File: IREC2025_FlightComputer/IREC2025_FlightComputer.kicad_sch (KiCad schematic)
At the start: 69 parts, among them J1 Molex Microfit, J2 BOOT0, J3 Companion, J5 SWD, Q1 SI7232DN-T1-GE3, U1 STM32U575VGTx, U2 NRVB120VLSFT1G, U4 NRVB120VLSFT1G, U5 LP5912Q3.3DRVRQ1, U8 TPS62153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

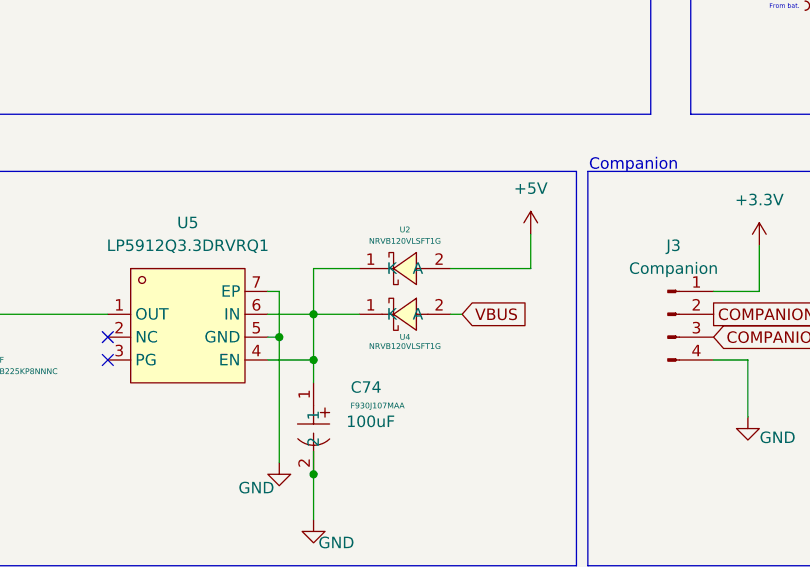
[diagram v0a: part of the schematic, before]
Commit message: Added silkscreen + Layout Minorchange
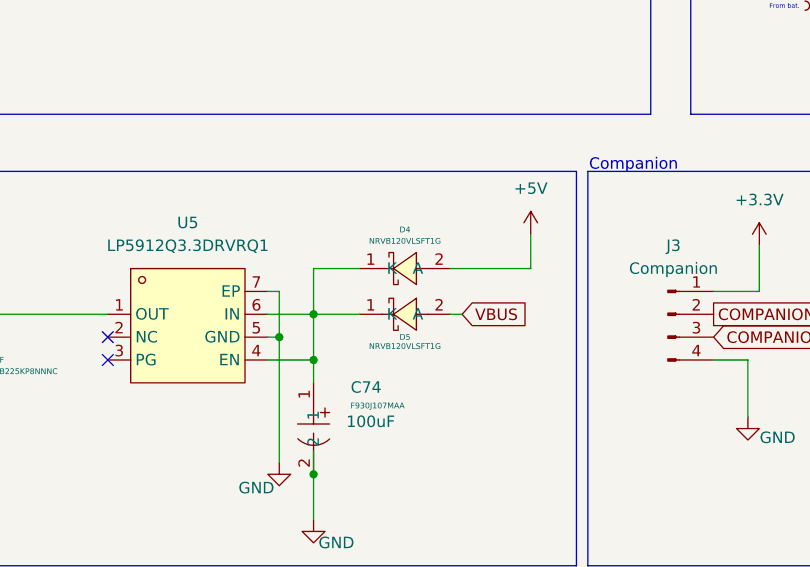
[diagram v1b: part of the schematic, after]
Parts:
- renumbered U2 to D4, U4 to D5
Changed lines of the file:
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@@
 		(on_board yes)
 		(dnp no)
-		(property "Reference" "U4"
+		(property "Reference" "D5"
 			(at 238.76 138.43 0)
 			(effects
@@
 			(project "IREC2025_FlightComputer"
 				(path "/d402aac1-6798-4745-a2ce-fc3f8e4c9afb"
-					(reference "U4")
+					(reference "D5")
 					(unit 1)
 				)
@@
 		(on_board yes)
 		(dnp no)
-		(property "Reference" "U2"
+		(property "Reference" "D4"
 			(at 238.76 126.492 0)
 			(effects
@@
 			(project ""
 				(path "/d402aac1-6798-4745-a2ce-fc3f8e4c9afb"
-					(reference "U2")
+					(reference "D4")
 					(unit 1)
 				)

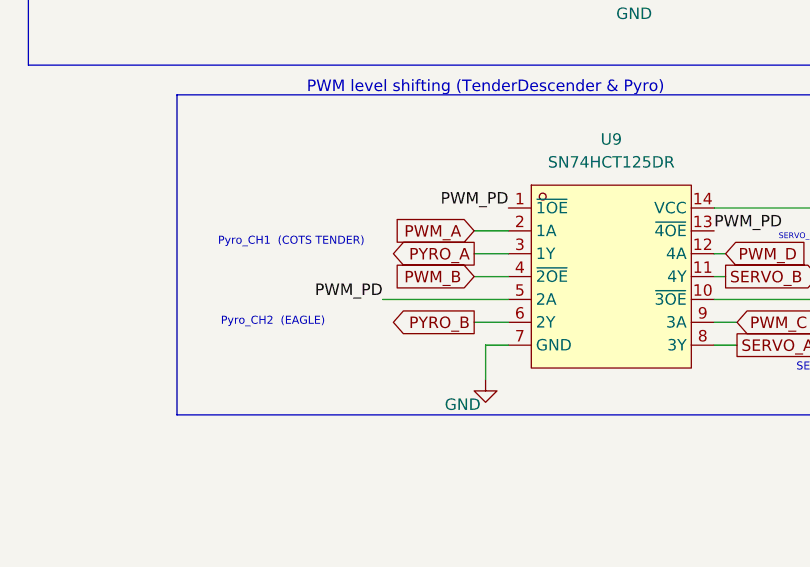
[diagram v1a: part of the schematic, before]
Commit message: Schematics minor fixes
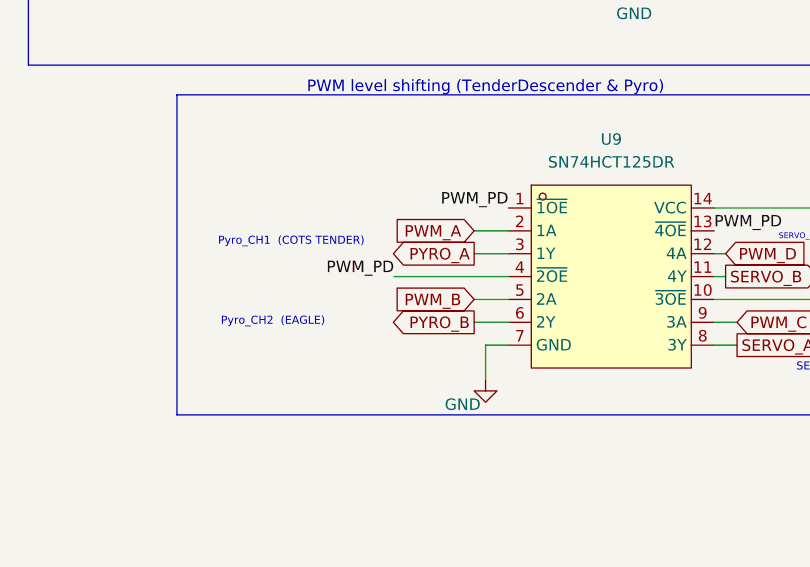
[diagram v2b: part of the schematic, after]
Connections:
- net PWM_B: now also U9.5 (2A); no longer U9.4 (~{2OE})
- net PWM_PD: now also U9.4 (~{2OE}); no longer U9.5 (2A)
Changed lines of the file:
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@@
 	(wire
 		(pts
-			(xy 52.07 212.09) (xy 66.04 212.09)
-		)
-		(stroke
-			(width 0)
-			(type default)
-		)
-	)
-	(wire
-		(pts
 			(xy 322.58 27.94) (xy 322.58 30.48)
 		)
@@
 	(wire
 		(pts
+			(xy 53.34 209.55) (xy 66.04 209.55)
+		)
+		(stroke
+			(width 0)
+			(type default)
+		)
+	)
+	(wire
+		(pts
 			(xy 182.88 104.14) (xy 182.88 106.68)
 		)
@@
 	(wire
 		(pts
-			(xy 62.23 209.55) (xy 66.04 209.55)
-		)
-		(stroke
-			(width 0)
-			(type default)
-		)
-	)
-	(wire
-		(pts
 			(xy 189.23 144.78) (xy 189.23 152.4)
 		)
@@
 	(wire
 		(pts
+			(xy 62.23 212.09) (xy 66.04 212.09)
+		)
+		(stroke
+			(width 0)
+			(type default)
+		)
+	)
+	(wire
+		(pts
 			(xy 121.92 213.36) (xy 121.92 215.9)
 		)
@@
 	)
 	(label "PWM_PD"
-		(at 52.07 212.09 180)
+		(at 53.34 209.55 180)
 		(effects
 			(font
@@
 	(global_label "PWM_B"
 		(shape input)
-		(at 62.23 209.55 180)
+		(at 62.23 212.09 180)
 		(fields_autoplaced yes)
 		(effects
@@
 		)
 		(property "Intersheetrefs" "${INTERSHEET_REFS}"
-			(at 52.8344 209.55 0)
+			(at 52.8344 212.09 0)
 			(effects
 				(font

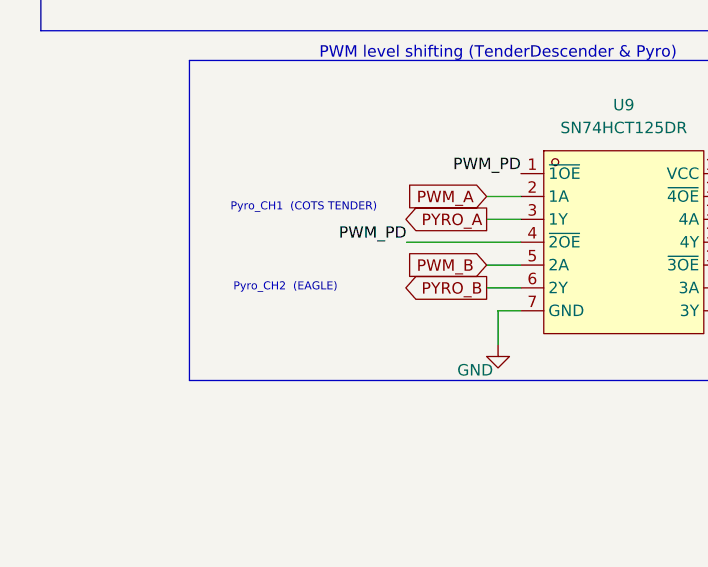
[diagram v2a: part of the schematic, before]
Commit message: USB Differentials matched to 90R
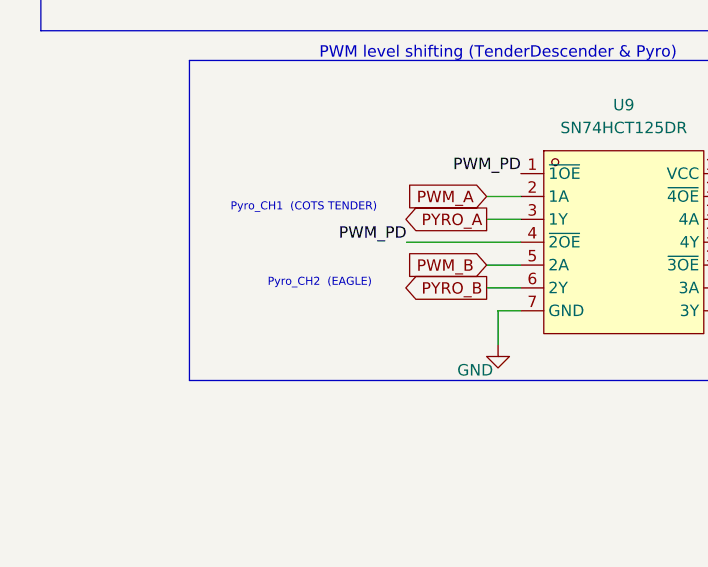
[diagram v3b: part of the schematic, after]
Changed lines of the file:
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@@
 	(text "Pyro_CH2  (EAGLE)"
 		(exclude_from_sim no)
-		(at 39.878 214.63 0)
+		(at 43.688 214.122 0)
 		(effects
 			(font

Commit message: forgor mmc int :( added
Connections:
- net MMC_INT: now reaches U1.61 (PD14)
- no-connect marks 25 -> 24
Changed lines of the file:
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@@
 	)
 	(no_connect
-		(at 57.15 142.24)
-	)
-	(no_connect
 		(at 57.15 66.04)
 	)
@@
 				(hide yes)
 			)
+		)
+	)
+	(global_label "MMC_INT"
+		(shape output)
+		(at 57.15 142.24 180)
+		(fields_autoplaced yes)
+		(effects
+			(font
+				(size 1.27 1.27)
+			)
+			(justify right)
+		)
+		(property "Intersheetrefs" "${INTERSHEET_REFS}"
+			(at 46.1215 142.24 0)
+			(effects
+				(font
+					(size 1.27 1.27)
+				)
+				(justify right)
+				(hide yes)
+			)

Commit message: changed most resistors to 0603
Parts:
- removed LED3: HS-0402-UR, EasyEDA:LED0402-R-RD, symbol EasyEDA:HS-0402-UR
- removed USB1: 10172013-00011LF, EasyEDA:USB-C-SMD_10174570-00A11LF, symbol EasyEDA:10172013-00011LF
- added LED3, LED4: QBLP617-AG1, PCM_JLCPCB:D_0603, symbol PCM_JLCPCB-Diodes:LED,0603,Red
- added R22: 1kΩ, PCM_JLCPCB:R_0603, symbol PCM_JLCPCB-Resistors:0402,1kΩ
- added USB1: Connector, USB-TYPE-C-16P, PCM_JLCPCB:TYPE-C-SMD_HX-TYPE-C-16PIN, symbol PCM_JLCPCB-Extended:Connector, USB-TYPE-C-16P
- C17: footprint PCM_JLCPCB:C_0402 -> PCM_JLCPCB:C_0603; name GRM155R71H104KE14D -> (none)
- R1: footprint PCM_JLCPCB:R_0402 -> PCM_JLCPCB:R_0603; name RC0402JR-0710KL -> RC0603JR-0710KL
- R10: footprint PCM_JLCPCB:R_0402 -> PCM_JLCPCB:R_0603; name RC0402JR-07100KL -> RC0603JR-07100KL
- R12, R13, R14, R15, R3, R39, R4: footprint PCM_JLCPCB:R_0402 -> PCM_JLCPCB:R_0603
- R2: footprint PCM_JLCPCB:R_0402 -> PCM_JLCPCB:R_0603; name RC0402FR-0747KL -> RC0603FR-0747KL
- R38, R9: footprint PCM_JLCPCB:R_0402 -> PCM_JLCPCB:R_0603; Name RC0402JR-0710KL -> RC0603JR-0710KL
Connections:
- net +3.3V: now also LED3.2
- net D+: now also USB1.A6 (D+), USB1.B6 (D+)
- net D-: now also USB1.A7 (D-), USB1.B7 (D-)
- net GND: now also R22.2, USB1.A12B1 (GND), USB1.B12A1 (GND)
- net VBUS: now also USB1.A9B4 (VBUS), USB1.B9A4 (VBUS)
- net at R3.2: now also USB1.A5 (CC1)
- net at R39.2: now also LED3.1
- net GPIO_TEST: now reaches U1.35 (PB0)
- net GPIO_TEST: now also LED4.2
- net at R4.2: now also USB1.B5 (CC2)
- net ANT_SW: no longer names the net of U1.46 (PE15)
- new net: LED4.1, R22.1
- no-connect marks 24 -> 25
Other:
- moved on the sheet: R3, R4
